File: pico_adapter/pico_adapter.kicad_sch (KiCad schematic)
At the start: 46 parts, among them J1 L77HDE15SD1CH4F, J2 AudioJack3, J4 ADD-ON, J5 AGND, J6 PWR_REF, Q1 Q_NMOS_DGS, Q2 Q_NMOS_DGS, SW1 SW_Push

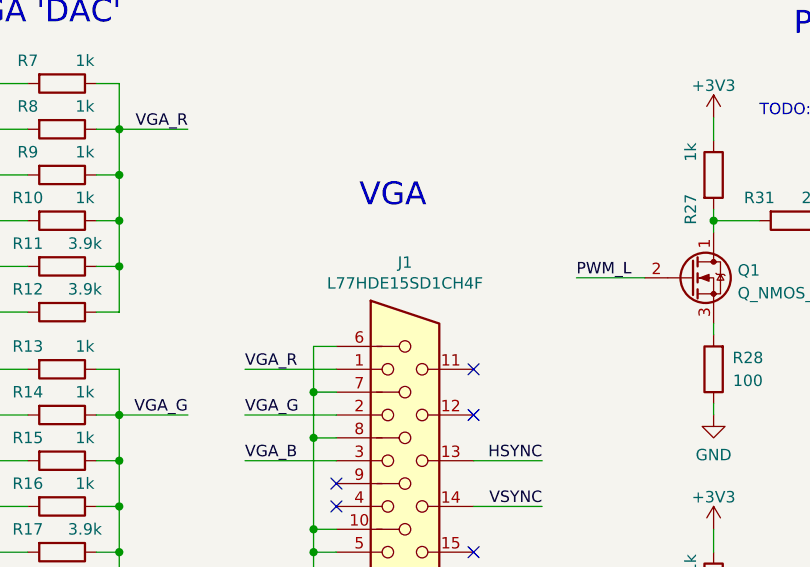
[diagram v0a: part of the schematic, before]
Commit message: changed VGA connector to more widely available variant + adjusted pcb design rules to JLC-PCB values
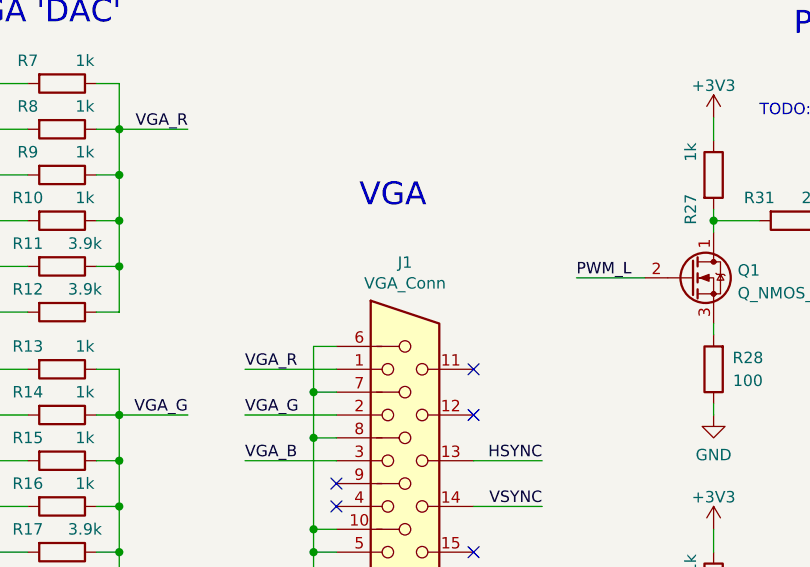
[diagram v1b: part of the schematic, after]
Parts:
- J1: value L77HDE15SD1CH4F -> VGA_Conn; footprint Connector_Dsub:DSUB-15-HD_Female_Horizontal_P2.29x1.98mm_EdgePinOffset8.35mm_Housed_MountingHolesOffset10.89mm -> VGA_connector:ICD15S13E4GV00LF
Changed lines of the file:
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@@
     (in_bom yes) (on_board yes)
     (property "Reference" "J1" (id 0) (at 179.07 45.2882 0))
-    (property "Value" "L77HDE15SD1CH4F" (id 1) (at 179.07 47.5996 0))
-    (property "Footprint" "Connector_Dsub:DSUB-15-HD_Female_Horizontal_P2.29x1.98mm_EdgePinOffset8.35mm_Housed_MountingHolesOffset10.89mm" (id 2) (at 154.94 57.15 0)
+    (property "Value" "VGA_Conn" (id 1) (at 179.07 47.5996 0))
+    (property "Footprint" "VGA_connector:ICD15S13E4GV00LF" (id 2) (at 154.94 57.15 0)
       (effects (font (size 1.27 1.27)) hide)
     )
-    (property "Datasheet" " ~" (id 3) (at 154.94 57.15 0)
+    (property "Datasheet" "ICD15S13E4GV00LF" (id 3) (at 154.94 57.15 0)
       (effects (font (size 1.27 1.27)) hide)
     )
@@
     )
     (path "/dfb90120-6b1d-4d5b-8348-783c21592827"
-      (reference "J1") (unit 1) (value "L77HDE15SD1CH4F") (footprint "Connector_Dsub:DSUB-15-HD_Female_Horizontal_P2.29x1.98mm_EdgePinOffset8.35mm_Housed_MountingHolesOffset10.89mm")
+      (reference "J1") (unit 1) (value "VGA_Conn") (footprint "VGA_connector:ICD15S13E4GV00LF")
     )
     (path "/25aafccc-32f1-4240-940f-ac8f7092ee50"
